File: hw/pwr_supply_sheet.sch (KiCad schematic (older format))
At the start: 19 parts

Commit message: pcb first revision created, ready to order
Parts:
- removed D201: DIODE_RS07J-GS18, usevolt:DO219AB, symbol DIODE_RS07J-GS18
- removed D205: WL-SMCW-150060BS75000-B, wurth_LEDS:0603, symbol WL-SMCW-150060BS75000-B
- removed R205: 470, multicomp:0603, symbol 470
- renumbered D202 to D201, D203 to D202, D204 to D203
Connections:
- net labels removed: EBER_VIN
- wire segments 43 -> 38
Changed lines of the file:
@@
 EESchema Schematic File Version 2
-LIBS:msb-rescue
 LIBS:kemet
 LIBS:multicomp
@@
 LIBS:power
 LIBS:elt21300_kicad
-LIBS:msb-cache
+LIBS:esb-cache
 EELAYER 26 0
 EELAYER END
 $Descr A4 11693 8268
 encoding utf-8
-Sheet 2 16
+Sheet 2 17
 Title "Power supply"
 Date "2016-08-20"
@@
 $EndComp
 $Comp
-L DIODE_TVS_SMBJ33A-TRDO-214AA D203
+L DIODE_TVS_SMBJ33A-TRDO-214AA D202
 U 1 1 57B820C1
 P 2800 4050
-F 0 "D203" V 2892 3982 45  0000 R CNN
+F 0 "D202" V 2892 3982 45  0000 R CNN
 F 1 "DIODE_TVS_SMBJ33A-TRDO-214AA" V 2750 4750 45  0000 R CNN
 F 2 "usevolt:DO-214AA" H 2830 4200 20  0001 C CNN
@@
 $EndComp
 $Comp
-L DIODE_RS07J-GS18 D204
+L DIODE_RS07J-GS18 D203
 U 1 1 57B82329
 P 6200 3950
-F 0 "D204" V 6150 3852 45  0000 R CNN
+F 0 "D203" V 6150 3852 45  0000 R CNN
 F 1 "DIODE_RS07J-GS18" H 6220 3890 45  0001 L BNN
 F 2 "usevolt:DO219AB" H 6230 4100 20  0001 C CNN
@@
 	0    1    1    0
 $EndComp
-$Comp
-L 470 R205
-U 1 1 57B82ADF
-P 8850 3850
-F 0 "R205" V 8858 3908 45  0000 L CNN
-F 1 "470" V 8942 3908 45  0000 L CNN
-F 2 "multicomp:0603" H 8880 4000 20  0001 C CNN
-F 3 "" H 8819 3889 60  0001 C CNN
-F 4 "9331239" H 9219 4289 60  0001 C CNN "1st Source Part Number"
-F 5 "Farnell" H 9119 4189 60  0001 C CNN "1st Source"
-F 6 "MC0063W06031470R" H 9019 4089 60  0001 C CNN "Manufacturer Part Number"
-F 7 "MULTICOMP" H 8919 3989 60  0001 C CNN "Manufacturer"
-	1    8850 3850
-	0    1    1    0
-$EndComp
-$Comp
-L WL-SMCW-150060BS75000-B D205
-U 1 1 57B82B6E
-P 8850 4200
-F 0 "D205" V 8850 4132 45  0000 R CNN
-F 1 "WL-SMCW-150060BS75000-B" H 9050 4300 45  0001 L BNN
-F 2 "wurth_LEDS:0603" H 8880 4350 20  0001 C CNN
-F 3 "http://www.farnell.com/datasheets/1911343.pdf?_ga=1.259491274.1948984246.1460023966" H 8650 4400 60  0001 C CNN
-F 4 "150060BS75000" H 9059 4403 60  0001 C CNN "Manufacturer Part Number"
-F 5 "2322069" H 9259 4603 60  0001 C CNN "1st Source Part Number"
-F 6 "Farnell" H 9159 4503 60  0001 C CNN "1st Source"
-F 7 "WURTH ELEKTRONIK" H 8959 4303 60  0001 C CNN "Manufacturer"
-	1    8850 4200
-	0    -1   -1   0
-$EndComp
-Wire Wire Line
-	8850 4100 8850 4050
-Wire Wire Line
-	2700 4300 8850 4300
 Wire Wire Line
 	8000 4300 8000 4250
@@
 Wire Wire Line
 	8600 4150 8600 4300
-Connection ~ 8600 4300
-Wire Wire Line
-	8850 3750 8600 3750
 Wire Wire Line
 	8600 3600 8600 3850
@@
 	1    0    0    -1
 $EndComp
-Connection ~ 8600 3750
 Wire Wire Line
 	1350 3850 1700 3850
@@
 Text HLabel 2650 2500 2    60   Output ~ 0
 VBATOUT
-$Comp
-L DIODE_RS07J-GS18 D202
-U 1 1 5896E2A2
-P 1900 3850
-F 0 "D202" H 1850 3990 45  0000 C CNN
-F 1 "DIODE_RS07J-GS18" H 1920 3790 45  0001 L BNN
-F 2 "usevolt:DO219AB" H 1930 4000 20  0001 C CNN
-F 3 "http://www.vishay.com/docs/85742/rs07b.pdf" H 1920 3870 60  0001 C CNN
-F 4 "1864882" H 2520 4470 60  0001 C CNN "2nd Source Part Number"
-F 5 "Digi-Key" H 2220 4170 60  0001 C CNN "1st Source"
-F 6 "Farnell" H 2420 4370 60  0001 C CNN "2nd Source"
-F 7 "RS07J-GS18" H 2120 4070 60  0001 C CNN "Manufacturer Part Number"
-F 8 "RS07J-GS18-ND" H 2320 4270 60  0001 C CNN "1st Source Part Number"
-F 9 "Vishay Semiconductor Diodes Division" H 2020 3970 60  0001 C CNN "Manufacturer"
-	1    1900 3850
-	1    0    0    -1
-$EndComp
 Wire Wire Line
 	2000 3850 2300 3850
@@
 Wire Wire Line
 	1350 2500 2650 2500
-Text HLabel 1350 2950 0    60   Input ~ 0
-EBER_VIN
+Wire Wire Line
+	8600 4300 2700 4300
 $Comp
 L DIODE_RS07J-GS18 D201
-U 1 1 58B8EE35
-P 1700 2950
-F 0 "D201" H 1650 3090 45  0000 C CNN
-F 1 "DIODE_RS07J-GS18" H 1720 2890 45  0001 L BNN
-F 2 "usevolt:DO219AB" H 1730 3100 20  0001 C CNN
-F 3 "http://www.vishay.com/docs/85742/rs07b.pdf" H 1720 2970 60  0001 C CNN
-F 4 "1864882" H 2320 3570 60  0001 C CNN "2nd Source Part Number"
-F 5 "Digi-Key" H 2020 3270 60  0001 C CNN "1st Source"
-F 6 "Farnell" H 2220 3470 60  0001 C CNN "2nd Source"
-F 7 "RS07J-GS18" H 1920 3170 60  0001 C CNN "Manufacturer Part Number"
-F 8 "RS07J-GS18-ND" H 2120 3370 60  0001 C CNN "1st Source Part Number"
-F 9 "Vishay Semiconductor Diodes Division" H 1820 3070 60  0001 C CNN "Manufacturer"
-	1    1700 2950
-	1    0    0    -1
-$EndComp
-Wire Wire Line
-	1350 2950 1500 2950
-Wire Wire Line
-	1800 2950 2100 2950
-Wire Wire Line
-	2100 2950 2100 3850
-Connection ~ 2100 3850
+U 1 1 5896E2A2
+P 1900 3850
+F 0 "D201" H 1850 3990 45  0000 C CNN
+F 1 "DIODE_RS07J-GS18" H 1920 3790 45  0001 L BNN
+F 2 "usevolt:DO219AB" H 1930 4000 20  0001 C CNN
+F 3 "http://www.vishay.com/docs/85742/rs07b.pdf" H 1920 3870 60  0001 C CNN
+F 4 "1864882" H 2520 4470 60  0001 C CNN "2nd Source Part Number"
+F 5 "Digi-Key" H 2220 4170 60  0001 C CNN "1st Source"
+F 6 "Farnell" H 2420 4370 60  0001 C CNN "2nd Source"
+F 7 "RS07J-GS18" H 2120 4070 60  0001 C CNN "Manufacturer Part Number"
+F 8 "RS07J-GS18-ND" H 2320 4270 60  0001 C CNN "1st Source Part Number"
+F 9 "Vishay Semiconductor Diodes Division" H 2020 3970 60  0001 C CNN "Manufacturer"
+	1    1900 3850
+	1    0    0    -1
+$EndComp
 $EndSCHEMATC

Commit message: tag 3.0.0 schematic drawing started
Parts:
- removed R203: 10K, multicomp:0603, symbol 10K
- removed R204: 1K, multicomp:0603, symbol 1K
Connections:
- net VDDSENSE renamed VDD_SENSE
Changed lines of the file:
@@
 Connection ~ 3400 3850
 Wire Wire Line
-	8600 4150 8600 4300
+	8600 4300 8600 4150
 Wire Wire Line
 	8600 3600 8600 3850
@@
 	6850 3600 6850 3850
 $Comp
-L +5V #PWR206
+L +5V #PWR07
 U 1 1 57B831F8
 P 6850 3600
-F 0 "#PWR206" H 6850 3450 50  0001 C CNN
+F 0 "#PWR07" H 6850 3450 50  0001 C CNN
 F 1 "+5V" H 6865 3773 50  0000 C CNN
 F 2 "" H 6850 3600 50  0000 C CNN
@@
 Connection ~ 6850 3750
 $Comp
-L +3V3 #PWR207
+L +3V3 #PWR08
 U 1 1 57B83259
 P 8600 3600
-F 0 "#PWR207" H 8600 3450 50  0001 C CNN
+F 0 "#PWR08" H 8600 3450 50  0001 C CNN
 F 1 "+3V3" H 8615 3773 50  0000 C CNN
 F 2 "" H 8600 3600 50  0000 C CNN
@@
 NoConn ~ 4550 4050
 $Comp
-L VDD #PWR204
+L VDD #PWR09
 U 1 1 57B9C56A
 P 3800 2100
-F 0 "#PWR204" H 3800 1950 50  0001 C CNN
+F 0 "#PWR09" H 3800 1950 50  0001 C CNN
 F 1 "VDD" H 3817 2273 50  0000 C CNN
 F 2 "" H 3800 2100 50  0000 C CNN
@@
 $EndComp
 $Comp
-L PWR_FLAG #FLG201
+L PWR_FLAG #FLG010
 U 1 1 57B9C59C
 P 3800 2300
-F 0 "#FLG201" H 3800 2395 50  0001 C CNN
+F 0 "#FLG010" H 3800 2395 50  0001 C CNN
 F 1 "PWR_FLAG" H 3800 2523 50  0000 C CNN
 F 2 "" H 3800 2300 50  0000 C CNN
@@
 	3800 2300 3800 2100
 $Comp
-L GND #PWR205
+L GND #PWR011
 U 1 1 57B9D351
 P 4300 2350
-F 0 "#PWR205" H 4300 2100 50  0001 C CNN
+F 0 "#PWR011" H 4300 2100 50  0001 C CNN
 F 1 "GND" H 4305 2177 50  0000 C CNN
 F 2 "" H 4300 2350 50  0000 C CNN
@@
 $EndComp
 $Comp
-L PWR_FLAG #FLG202
+L PWR_FLAG #FLG012
 U 1 1 57B9D3A1
 P 4300 2150
-F 0 "#FLG202" H 4300 2245 50  0001 C CNN
+F 0 "#FLG012" H 4300 2245 50  0001 C CNN
 F 1 "PWR_FLAG" H 4300 2374 50  0000 C CNN
 F 2 "" H 4300 2150 50  0000 C CNN
@@
 	4300 2150 4300 2350
 $Comp
-L GND #PWR203
+L GND #PWR013
 U 1 1 57CF1F5E
 P 2800 4500
-F 0 "#PWR203" H 2800 4250 50  0001 C CNN
+F 0 "#PWR013" H 2800 4250 50  0001 C CNN
 F 1 "GND" H 2805 4327 50  0000 C CNN
 F 2 "" H 2800 4500 50  0000 C CNN
@@
 	1    0    0    -1
 $EndComp
-Text HLabel 1350 2500 0    60   Input ~ 0
-VBATIN
-Text HLabel 2650 2500 2    60   Output ~ 0
-VBATOUT
 Wire Wire Line
 	2000 3850 2300 3850
-$Comp
-L 10K R201
-U 1 1 58970B58
-P 1600 4050
-F 0 "R201" V 1608 4108 45  0000 L CNN
-F 1 "10K" V 1692 4108 45  0000 L CNN
-F 2 "multicomp:0603" H 1630 4200 20  0001 C CNN
-F 3 "http://www.farnell.com/datasheets/1788326.pdf?_ga=1.214208087.1948984246.1460023966" H 1569 4089 60  0001 C CNN
-F 4 "9330399" H 1969 4489 60  0001 C CNN "1st Source Part Number"
-F 5 "Farnell" H 1869 4389 60  0001 C CNN "1st Source"
-F 6 "MC0063W0603110K" H 1769 4289 60  0001 C CNN "Manufacturer Part Number"
-F 7 "MULTICOMP" H 1669 4189 60  0001 C CNN "Manufacturer"
-	1    1600 4050
-	0    1    1    0
-$EndComp
-$Comp
-L 1K R202
-U 1 1 58970BDD
-P 1600 4400
-F 0 "R202" V 1608 4458 45  0000 L CNN
-F 1 "1K" V 1692 4458 45  0000 L CNN
-F 2 "multicomp:0603" H 1630 4550 20  0001 C CNN
-F 3 "" H 1569 4439 60  0001 C CNN
-F 4 "9330380" H 1969 4839 60  0001 C CNN "1st Source Part Number"
-F 5 "Farnell" H 1869 4739 60  0001 C CNN "1st Source"
-F 6 "MC0063W060311K" H 1769 4639 60  0001 C CNN "Manufacturer Part Number"
-F 7 "MULTICOMP" H 1669 4539 60  0001 C CNN "Manufacturer"
-	1    1600 4400
-	0    1    1    0
-$EndComp
-Wire Wire Line
-	1600 4300 1600 4250
-Wire Wire Line
-	1600 3950 1600 3850
-Connection ~ 1600 3850
-$Comp
-L GND #PWR201
-U 1 1 58970E5F
-P 1600 4650
-F 0 "#PWR201" H 1600 4400 50  0001 C CNN
-F 1 "GND" H 1605 4477 50  0000 C CNN
-F 2 "" H 1600 4650 50  0000 C CNN
-F 3 "" H 1600 4650 50  0000 C CNN
-	1    1600 4650
-	1    0    0    -1
-$EndComp
-Wire Wire Line
-	1600 4650 1600 4600
-Wire Wire Line
-	1600 4250 1850 4250
-Text HLabel 1850 4250 2    60   Output ~ 0
-VDDSENSE
-$Comp
-L 10K R203
-U 1 1 5897141A
-P 2400 2650
-F 0 "R203" V 2408 2708 45  0000 L CNN
-F 1 "10K" V 2492 2708 45  0000 L CNN
-F 2 "multicomp:0603" H 2430 2800 20  0001 C CNN
-F 3 "http://www.farnell.com/datasheets/1788326.pdf?_ga=1.214208087.1948984246.1460023966" H 2369 2689 60  0001 C CNN
-F 4 "9330399" H 2769 3089 60  0001 C CNN "1st Source Part Number"
-F 5 "Farnell" H 2669 2989 60  0001 C CNN "1st Source"
-F 6 "MC0063W0603110K" H 2569 2889 60  0001 C CNN "Manufacturer Part Number"
-F 7 "MULTICOMP" H 2469 2789 60  0001 C CNN "Manufacturer"
-	1    2400 2650
-	0    1    1    0
-$EndComp
-$Comp
-L 1K R204
-U 1 1 5897148B
-P 2400 3000
-F 0 "R204" V 2408 3058 45  0000 L CNN
-F 1 "1K" V 2492 3058 45  0000 L CNN
-F 2 "multicomp:0603" H 2430 3150 20  0001 C CNN
-F 3 "" H 2369 3039 60  0001 C CNN
-F 4 "9330380" H 2769 3439 60  0001 C CNN "1st Source Part Number"
-F 5 "Farnell" H 2669 3339 60  0001 C CNN "1st Source"
-F 6 "MC0063W060311K" H 2569 3239 60  0001 C CNN "Manufacturer Part Number"
-F 7 "MULTICOMP" H 2469 3139 60  0001 C CNN "Manufacturer"
-	1    2400 3000
-	0    1    1    0
-$EndComp
-$Comp
-L GND #PWR202
-U 1 1 58971507
-P 2400 3250
-F 0 "#PWR202" H 2400 3000 50  0001 C CNN
-F 1 "GND" H 2405 3077 50  0000 C CNN
-F 2 "" H 2400 3250 50  0000 C CNN
-F 3 "" H 2400 3250 50  0000 C CNN
-	1    2400 3250
-	1    0    0    -1
-$EndComp
-Wire Wire Line
-	2400 3250 2400 3200
-Wire Wire Line
-	2400 2900 2400 2850
-Wire Wire Line
-	2400 2550 2400 2500
-Connection ~ 2400 2500
-Wire Wire Line
-	2400 2850 2650 2850
-Text HLabel 2650 2850 2    60   Output ~ 0
-VBATSENSE
-Wire Wire Line
-	1350 2500 2650 2500
-Wire Wire Line
-	8600 4300 2700 4300
+Wire Wire Line
+	2700 4300 8600 4300
 $Comp
 L DIODE_RS07J-GS18 D201
@@
 	1    0    0    -1
 $EndComp
+$Comp
+L 10K R201
+U 1 1 59B1277F
+P 1600 4050
+F 0 "R201" V 1608 4108 45  0000 L CNN
+F 1 "10K" V 1692 4108 45  0000 L CNN
+F 2 "multicomp:0603" H 1630 4200 20  0001 C CNN
+F 3 "http://www.farnell.com/datasheets/1788326.pdf?_ga=1.214208087.1948984246.1460023966" H 1569 4089 60  0001 C CNN
+F 4 "9330399" H 1969 4489 60  0001 C CNN "1st Source Part Number"
+F 5 "Farnell" H 1869 4389 60  0001 C CNN "1st Source"
+F 6 "MC0063W0603110K" H 1769 4289 60  0001 C CNN "Manufacturer Part Number"
+F 7 "MULTICOMP" H 1669 4189 60  0001 C CNN "Manufacturer"
+	1    1600 4050
+	0    1    1    0
+$EndComp
+$Comp
+L 1K R202
+U 1 1 59B12803
+P 1600 4450
+F 0 "R202" V 1608 4508 45  0000 L CNN
+F 1 "1K" V 1692 4508 45  0000 L CNN
+F 2 "multicomp:0603" H 1630 4600 20  0001 C CNN
+F 3 "" H 1569 4489 60  0001 C CNN
+F 4 "9330380" H 1969 4889 60  0001 C CNN "1st Source Part Number"
+F 5 "Farnell" H 1869 4789 60  0001 C CNN "1st Source"
+F 6 "MC0063W060311K" H 1769 4689 60  0001 C CNN "Manufacturer Part Number"
+F 7 "MULTICOMP" H 1669 4589 60  0001 C CNN "Manufacturer"
+	1    1600 4450
+	0    1    1    0
+$EndComp
+$Comp
+L GND #PWR014
+U 1 1 59B128CC
+P 1600 4750
+F 0 "#PWR014" H 1600 4500 50  0001 C CNN
+F 1 "GND" H 1605 4577 50  0000 C CNN
+F 2 "" H 1600 4750 50  0000 C CNN
+F 3 "" H 1600 4750 50  0000 C CNN
+	1    1600 4750
+	1    0    0    -1
+$EndComp
+Wire Wire Line
+	1600 4750 1600 4650
+Wire Wire Line
+	1600 4250 1600 4350
+Wire Wire Line
+	1600 3950 1600 3850
+Connection ~ 1600 3850
+Wire Wire Line
+	1600 4300 1700 4300
+Connection ~ 1600 4300
+Text HLabel 1700 4300 2    60   Output ~ 0
+VDD_SENSE
 $EndSCHEMATC

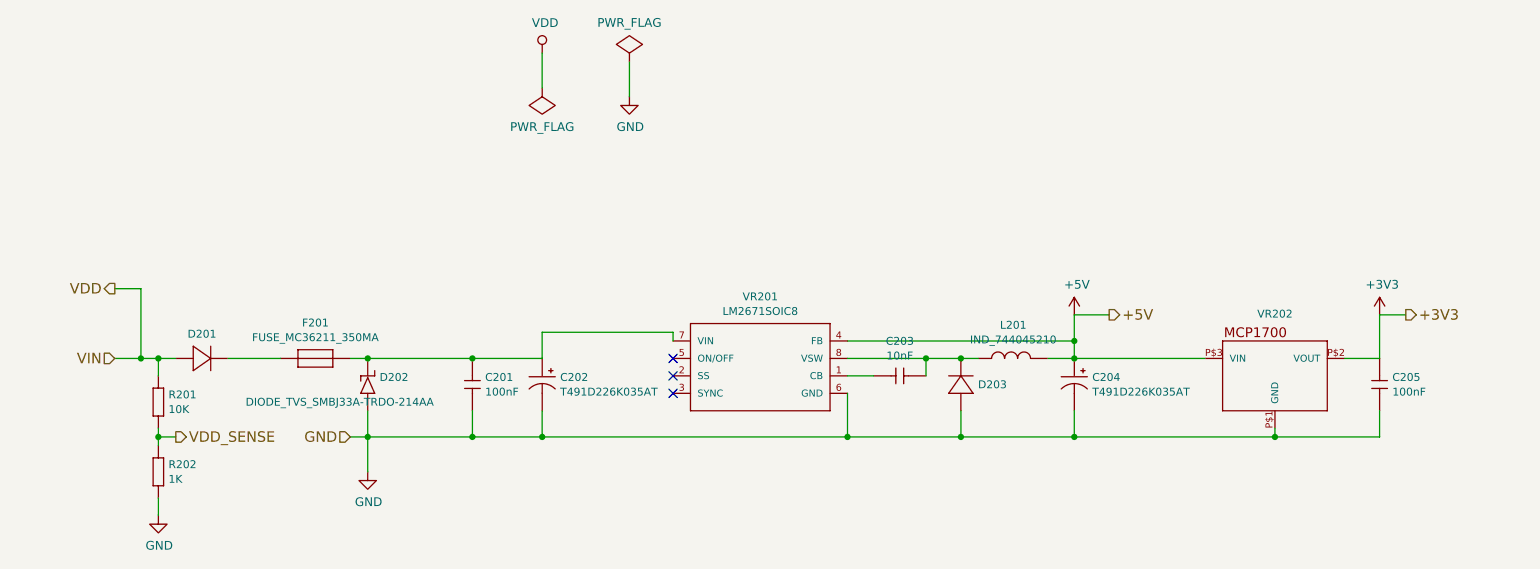
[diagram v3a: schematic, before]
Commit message: added binary and build files to gitignore
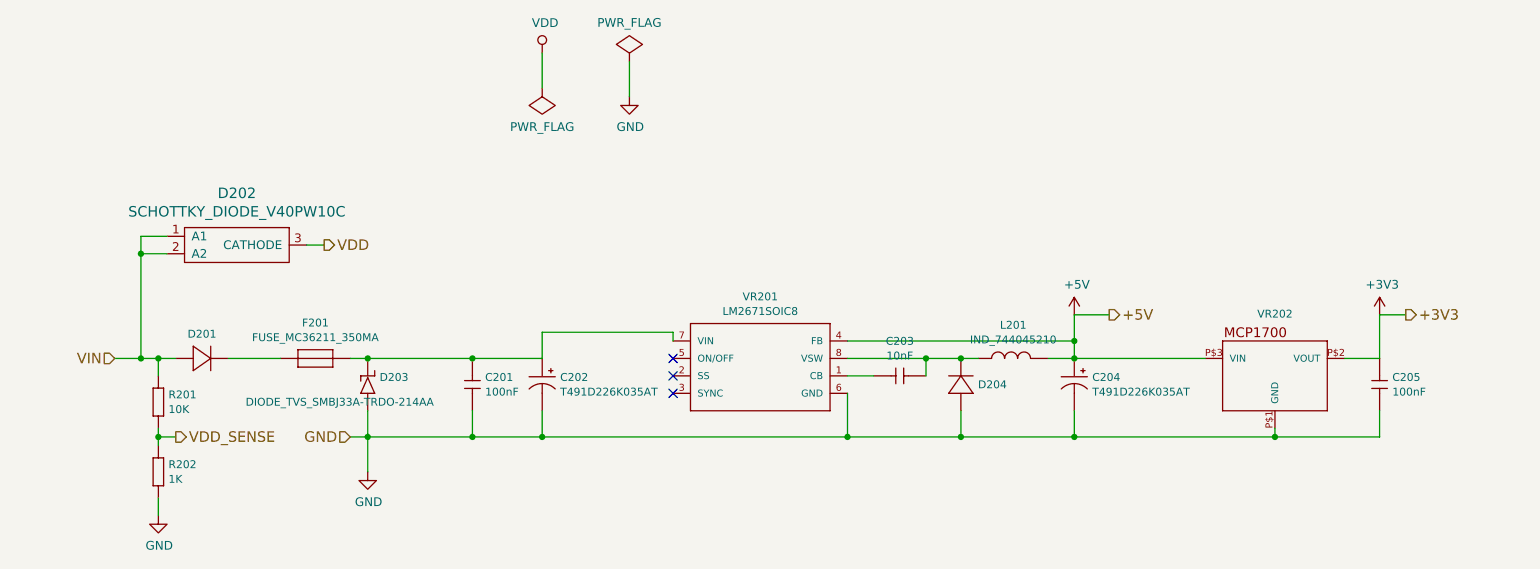
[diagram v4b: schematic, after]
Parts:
- added D202: SCHOTTKY_DIODE_V40PW10C, usevolt:SlimDPAK, symbol SCHOTTKY_DIODE_V40PW10C
- renumbered D202 to D203, D203 to D204
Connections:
- net VDD: now also D202.3 (CATHODE); no longer D201.P$1 (P), R201.2 (R2)
- new net VIN: D201.P$1 (P), D202.1 (A1), D202.2 (A2), R201.2 (R2)
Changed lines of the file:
@@
 $EndComp
 $Comp
-L DIODE_TVS_SMBJ33A-TRDO-214AA D202
+L DIODE_TVS_SMBJ33A-TRDO-214AA D203
 U 1 1 57B820C1
 P 2800 4050
-F 0 "D202" V 2892 3982 45  0000 R CNN
+F 0 "D203" V 2892 3982 45  0000 R CNN
 F 1 "DIODE_TVS_SMBJ33A-TRDO-214AA" V 2750 4750 45  0000 R CNN
 F 2 "usevolt:DO-214AA" H 2830 4200 20  0001 C CNN
@@
 $EndComp
 $Comp
-L DIODE_RS07J-GS18 D203
+L DIODE_RS07J-GS18 D204
 U 1 1 57B82329
 P 6200 3950
-F 0 "D203" V 6150 3852 45  0000 R CNN
+F 0 "D204" V 6150 3852 45  0000 R CNN
 F 1 "DIODE_RS07J-GS18" H 6220 3890 45  0001 L BNN
 F 2 "usevolt:DO219AB" H 6230 4100 20  0001 C CNN
@@
 	6850 3600 6850 3850
 $Comp
-L +5V #PWR07
+L +5V #PWR06
 U 1 1 57B831F8
 P 6850 3600
-F 0 "#PWR07" H 6850 3450 50  0001 C CNN
+F 0 "#PWR06" H 6850 3450 50  0001 C CNN
 F 1 "+5V" H 6865 3773 50  0000 C CNN
 F 2 "" H 6850 3600 50  0000 C CNN
@@
 Connection ~ 6850 3750
 $Comp
-L +3V3 #PWR08
+L +3V3 #PWR07
 U 1 1 57B83259
 P 8600 3600
-F 0 "#PWR08" H 8600 3450 50  0001 C CNN
+F 0 "#PWR07" H 8600 3450 50  0001 C CNN
 F 1 "+3V3" H 8615 3773 50  0000 C CNN
 F 2 "" H 8600 3600 50  0000 C CNN
@@
 Wire Wire Line
 	8750 3600 8600 3600
-Text HLabel 1350 3450 0    60   Output ~ 0
+Text HLabel 2550 3200 2    60   Output ~ 0
 VDD
 Text HLabel 2700 4300 0    60   Input ~ 0
@@
 NoConn ~ 4550 4050
 $Comp
-L VDD #PWR09
+L VDD #PWR08
 U 1 1 57B9C56A
 P 3800 2100
-F 0 "#PWR09" H 3800 1950 50  0001 C CNN
+F 0 "#PWR08" H 3800 1950 50  0001 C CNN
 F 1 "VDD" H 3817 2273 50  0000 C CNN
 F 2 "" H 3800 2100 50  0000 C CNN
@@
 $EndComp
 $Comp
-L PWR_FLAG #FLG010
+L PWR_FLAG #FLG09
 U 1 1 57B9C59C
 P 3800 2300
-F 0 "#FLG010" H 3800 2395 50  0001 C CNN
+F 0 "#FLG09" H 3800 2395 50  0001 C CNN
 F 1 "PWR_FLAG" H 3800 2523 50  0000 C CNN
 F 2 "" H 3800 2300 50  0000 C CNN
@@
 	3800 2300 3800 2100
 $Comp
-L GND #PWR011
+L GND #PWR010
 U 1 1 57B9D351
 P 4300 2350
-F 0 "#PWR011" H 4300 2100 50  0001 C CNN
+F 0 "#PWR010" H 4300 2100 50  0001 C CNN
 F 1 "GND" H 4305 2177 50  0000 C CNN
 F 2 "" H 4300 2350 50  0000 C CNN
@@
 $EndComp
 $Comp
-L PWR_FLAG #FLG012
+L PWR_FLAG #FLG011
 U 1 1 57B9D3A1
 P 4300 2150
-F 0 "#FLG012" H 4300 2245 50  0001 C CNN
+F 0 "#FLG011" H 4300 2245 50  0001 C CNN
 F 1 "PWR_FLAG" H 4300 2374 50  0000 C CNN
 F 2 "" H 4300 2150 50  0000 C CNN
@@
 	4300 2150 4300 2350
 $Comp
-L GND #PWR013
+L GND #PWR012
 U 1 1 57CF1F5E
 P 2800 4500
-F 0 "#PWR013" H 2800 4250 50  0001 C CNN
+F 0 "#PWR012" H 2800 4250 50  0001 C CNN
 F 1 "GND" H 2805 4327 50  0000 C CNN
 F 2 "" H 2800 4500 50  0000 C CNN
@@
 Wire Wire Line
 	3800 3850 3800 3700
-Wire Wire Line
-	1350 3450 1500 3450
-Wire Wire Line
-	1500 3450 1500 3850
 Connection ~ 1500 3850
 Wire Wire Line
@@
 $EndComp
 $Comp
-L GND #PWR014
+L GND #PWR013
 U 1 1 59B128CC
 P 1600 4750
-F 0 "#PWR014" H 1600 4500 50  0001 C CNN
+F 0 "#PWR013" H 1600 4500 50  0001 C CNN
 F 1 "GND" H 1605 4577 50  0000 C CNN
 F 2 "" H 1600 4750 50  0000 C CNN
@@
 Text HLabel 1700 4300 2    60   Output ~ 0
 VDD_SENSE
+$Comp
+L SCHOTTKY_DIODE_V40PW10C D202
+U 1 1 59B7B8B2
+P 2050 3250
+F 0 "D202" H 2050 3597 60  0000 C CNN
+F 1 "SCHOTTKY_DIODE_V40PW10C" H 2050 3491 60  0000 C CNN
+F 2 "usevolt:SlimDPAK" H 1850 2900 60  0001 C CNN
+F 3 "http://www.farnell.com/datasheets/2245239.pdf?_ga=2.16591231.874534928.1505194133-1862443086.1504075057" H 1850 2900 60  0001 C CNN
+F 4 "2535169" H 2400 3850 60  0001 C CNN "1st Source Part Number"
+F 5 "Digikey" H 2500 3950 60  0001 C CNN "2nd Source"
+F 6 "Farnell" H 2300 3750 60  0001 C CNN "1st Source"
+F 7 "V40PW10CHM3/I" H 2200 3650 60  0001 C CNN "Manufacturer Part Number"
+F 8 "V40PW10CHM3/IGICT-ND" H 2600 4050 60  0001 C CNN "2nd Source Part Number"
+F 9 "VISHAY" H 2100 3550 60  0001 C CNN "Manufacturer"
+	1    2050 3250
+	1    0    0    -1
+$EndComp
+Wire Wire Line
+	2550 3200 2450 3200
+Wire Wire Line
+	1500 3850 1500 3150
+Wire Wire Line
+	1500 3150 1650 3150
+Wire Wire Line
+	1650 3250 1500 3250
+Connection ~ 1500 3250
 $EndSCHEMATC
